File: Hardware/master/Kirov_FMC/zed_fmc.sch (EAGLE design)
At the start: 1 part

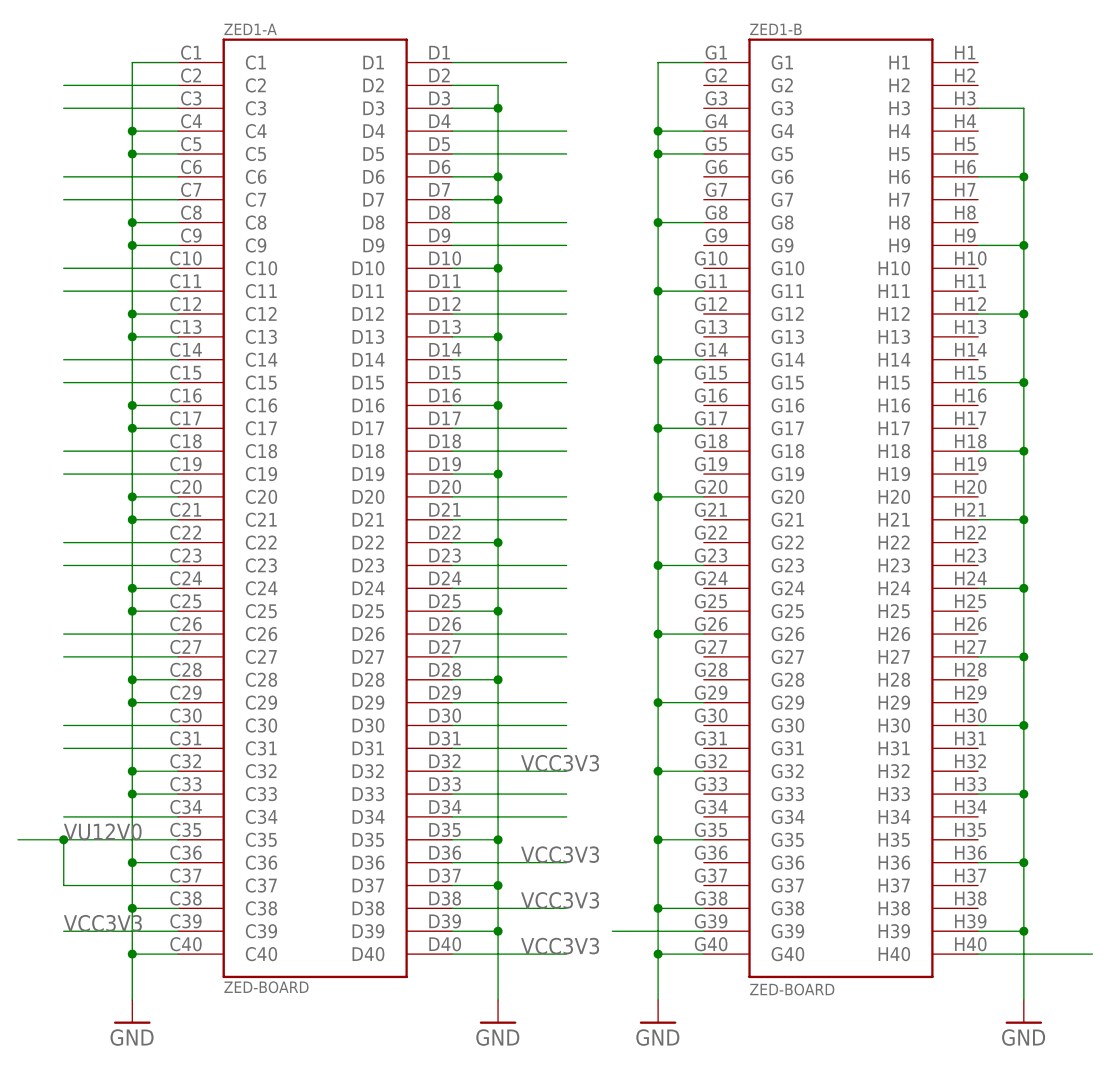
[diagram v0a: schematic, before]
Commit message: Updated zed_fmc with nets
This is partial commit.
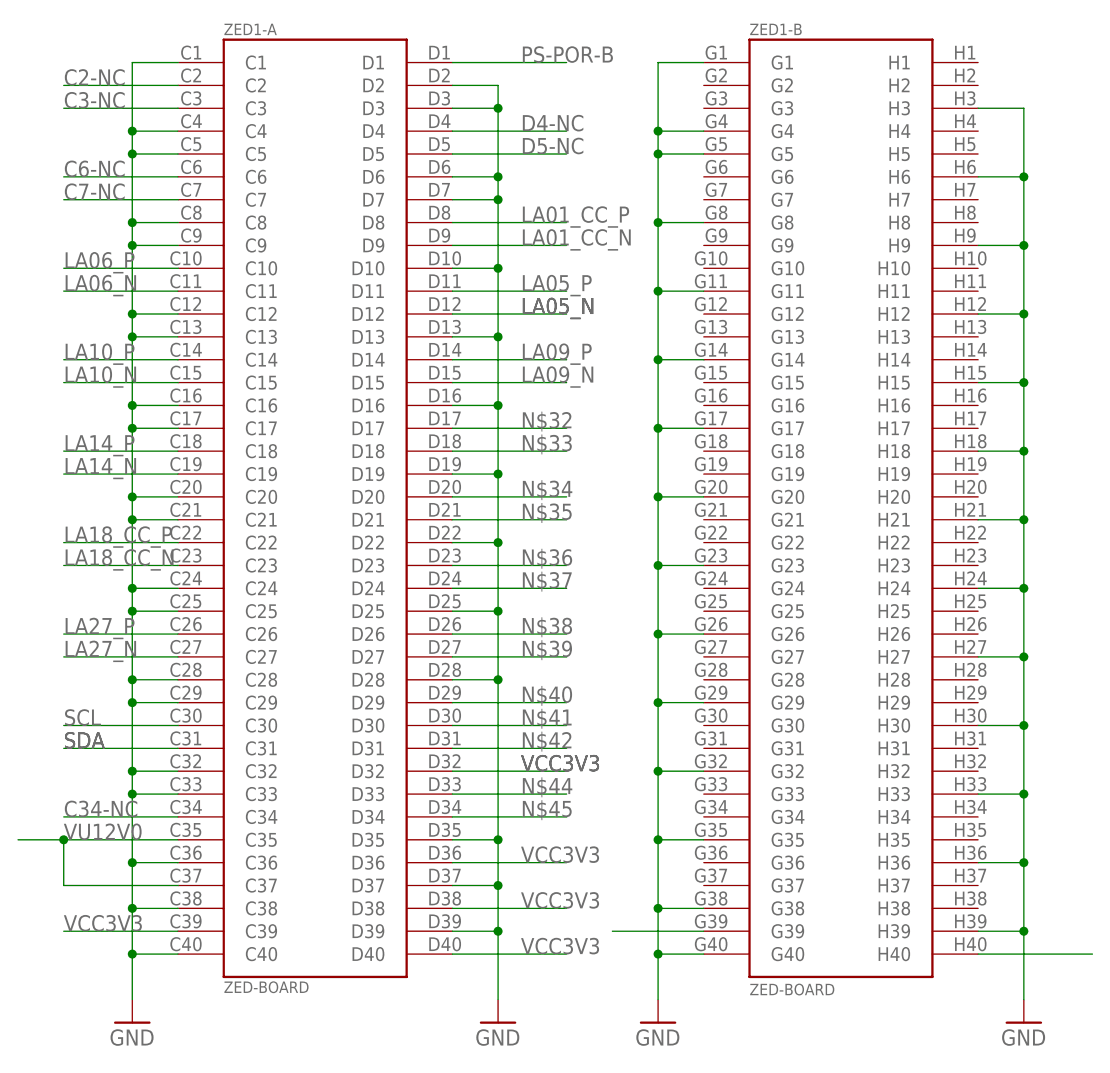
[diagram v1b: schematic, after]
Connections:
- net N$10 renamed LA10_N
- net N$11 renamed LA14_P
- net N$12 renamed LA14_N
- net N$13 renamed LA18_CC_P
- net N$14 renamed LA18_CC_N
- net N$15 renamed LA27_P
- net N$16 renamed LA27_N
- net N$17 renamed SCL
- net N$18 renamed SDA
- net N$19 renamed C34-NC
- net N$23 renamed PS-POR-B
- net N$24 renamed D4-NC
- net N$25 renamed D5-NC
- net N$26 renamed LA01_CC_P
- net N$27 renamed LA01_CC_N
- net N$28 renamed LA05_P
- net N$29 renamed LA05_N
- net N$3 renamed C2-NC
- net N$30 renamed LA09_P
- net N$31 renamed LA09_N
- net N$4 renamed C3-NC
- net N$5 renamed C6-NC
- net N$6 renamed C7-NC
- net N$7 renamed LA06_P
- net N$8 renamed LA06_N
- net N$9 renamed LA10_P
